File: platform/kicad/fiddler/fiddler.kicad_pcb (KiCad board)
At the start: 2 copper layers, 80 x 78.8 mm, 141 parts, among them J1 5033981892, J2 12402012E212A, J3 Conn_01x04_Pin, J4 Screw_Terminal_01x02, Q1 NPN, Q2 NPN, SW1 SW_Push, SW2 SW_Push, SW3 SW_Push, T1 PT61018PEL, U1 ESP32-WROOM-32E, U2 TAS5731MPHP, U3 LAN8720A, U4 MCP16311x-xMNY, U5 CP2102N-Axx-xQFN24, U6 AP63203WU

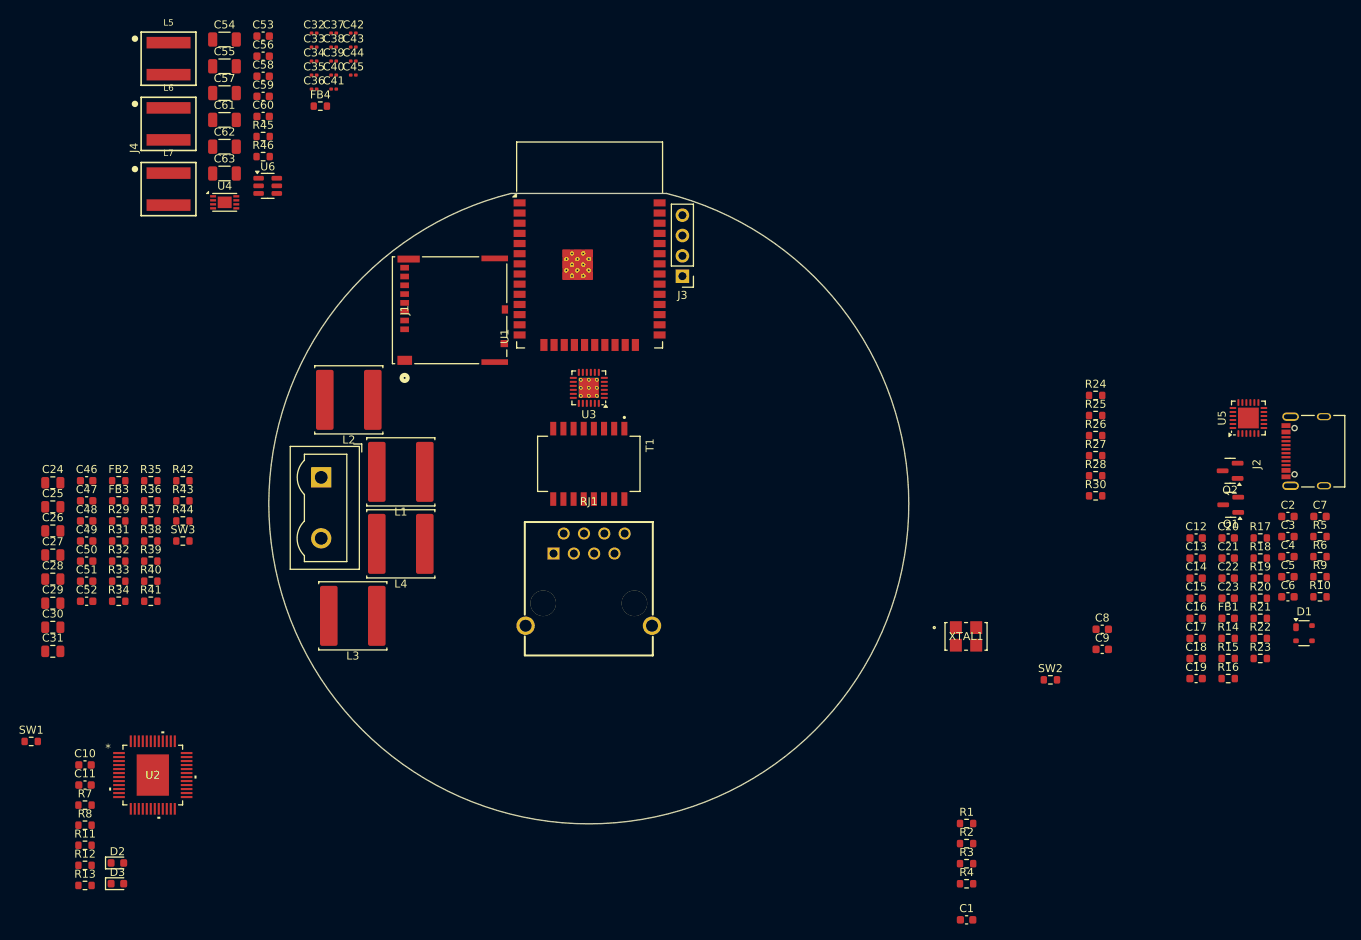
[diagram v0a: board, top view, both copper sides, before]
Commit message: Fiddler Ray Speaker: Complete first revision
This change completes the first iteration schematic and layout for the fiddler ray speaker PCB.
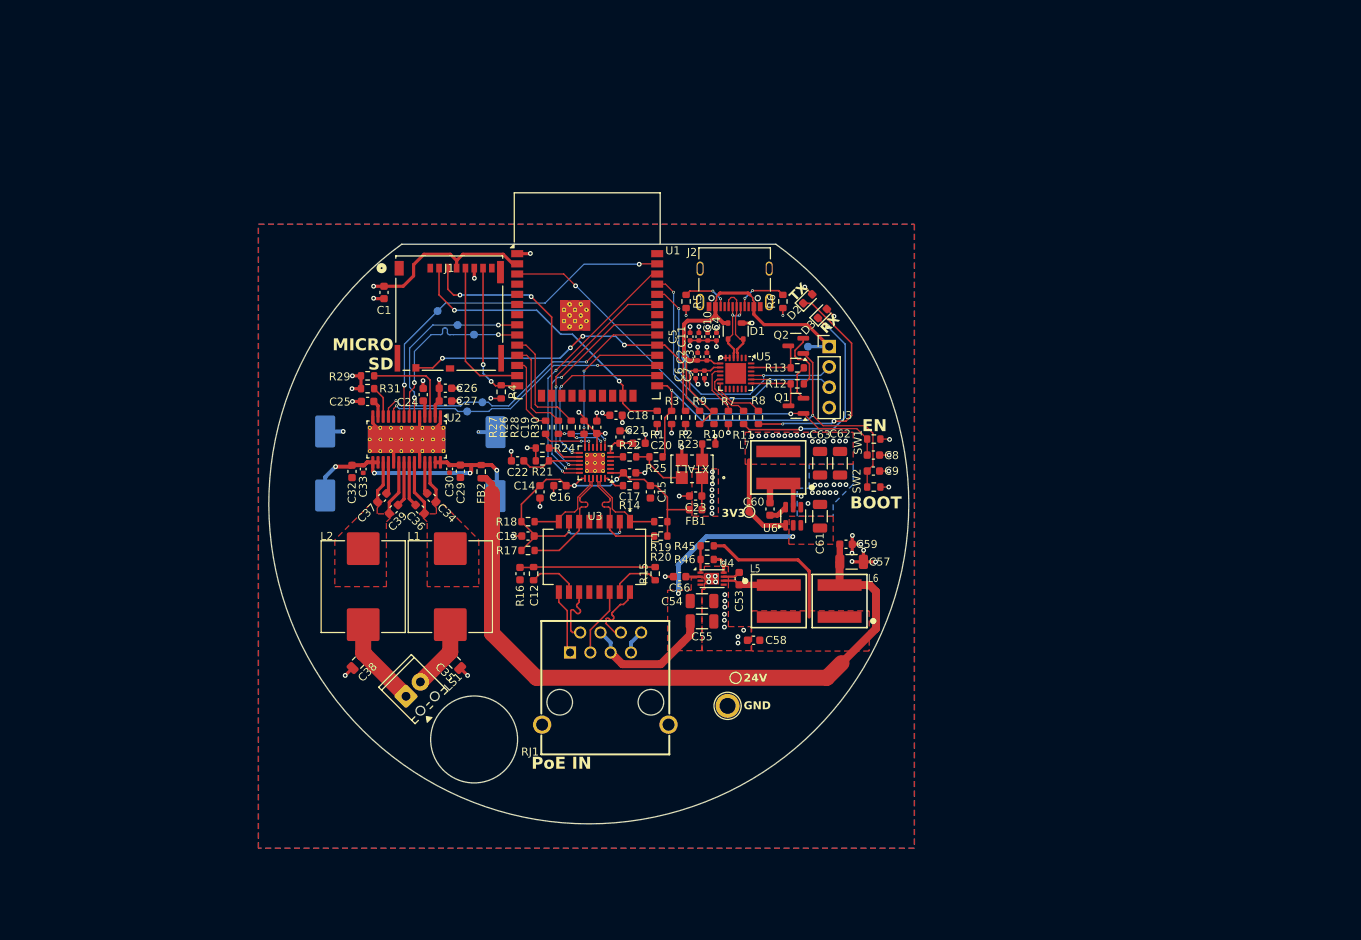
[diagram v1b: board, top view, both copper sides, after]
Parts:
- removed C40, C45: 680n, Capacitor_SMD:C_0201_0603Metric
- removed C41: 4n7, Capacitor_SMD:C_0201_0603Metric
- removed C42, C44: 330p, Capacitor_SMD:C_0201_0603Metric
- removed C43: 2.2n, Capacitor_SMD:C_0201_0603Metric
- removed C46, C48, C50, C51: 100n 10V, Capacitor_SMD:C_0603_1608Metric
- removed C47: 10u 16V, Capacitor_SMD:C_0603_1608Metric
- removed C49: 4u7 6.3V, Capacitor_SMD:C_0603_1608Metric
- removed C52: 1u 25V, Capacitor_SMD:C_0603_1608Metric
- removed FB3, FB4: 120/4A, Resistor_SMD:R_0603_1608Metric
- removed J4: Screw_Terminal_01x02, TerminalBlock:TerminalBlock_Wuerth_691311400102_P7.62mm
- removed L3, L4: 15u, Inductor_SMD:L_Changjiang_FNR8040S
- removed R32, R33, R35, R39: 10k, Resistor_SMD:R_0603_1608Metric
- removed R34: 15k, Resistor_SMD:R_0603_1608Metric
- removed R36: 18k2 1%, Resistor_SMD:R_0603_1608Metric
- removed R37, R38, R42, R43: 18, Resistor_SMD:R_0603_1608Metric
- removed R40, R41: 470, Resistor_SMD:R_0603_1608Metric
- removed R44: 0, Resistor_SMD:R_0603_1608Metric
- removed SW3: SW_Push, Resistor_SMD:R_0603_1608Metric
- added LS1: Speaker, TerminalBlock_Phoenix:TerminalBlock_Phoenix_MPT-0,5-2-2.54_1x02_P2.54mm_Horizontal, F.Cu at (77.2, 124.1)
- added TP1: 24, TestPoint:TestPoint_Pad_D1.0mm, F.Cu at (118.3, 121.8)
- added TP10: SDA, TestPoint:TestPoint_Pad_D1.0mm, B.Cu at (84.8, 88.5)
- added TP2: GND, TestPoint:TestPoint_Plated_Hole_D2.0mm, F.Cu at (117.3, 125.2)
- added TP3: 3V3, TestPoint:TestPoint_Pad_D1.0mm, F.Cu at (120.0, 101.0)
- added TP4: VBUS, TestPoint:TestPoint_Pad_D1.0mm, B.Cu at (127.4, 80.3)
- added TP5: 2V7, TestPoint:TestPoint_Pad_D1.0mm, B.Cu at (112.0, 81.7)
- added TP6: LRCLK, TestPoint:TestPoint_Pad_D1.0mm, B.Cu at (83.6, 77.7)
- added TP7: BLCK, TestPoint:TestPoint_Pad_D1.0mm, B.Cu at (85.7, 78.8)
- added TP8: SDIN, TestPoint:TestPoint_Pad_D1.0mm, B.Cu at (81.1, 75.9)
- added TP9: SCL, TestPoint:TestPoint_Pad_D1.0mm, B.Cu at (86.7, 87.3)
- C10, C11, C2, C3, C4, C5, C6, C7: footprint Capacitor_SMD:C_0603_1608Metric -> Capacitor_SMD:C_0402_1005Metric
- C24: value 100n 50V -> 1u; footprint Capacitor_SMD:C_0805_2012Metric -> Capacitor_SMD:C_0603_1608Metric
- C25: value 220u 35V -> 1u; footprint Capacitor_SMD:C_0805_2012Metric -> Capacitor_SMD:C_0603_1608Metric
- C26: value 100n 50V -> 4u7; footprint Capacitor_SMD:C_0805_2012Metric -> Capacitor_SMD:C_0603_1608Metric
- C27: value 220u 35V -> 100n; footprint Capacitor_SMD:C_0805_2012Metric -> Capacitor_SMD:C_0603_1608Metric
- C28, C31: value 33n -> 390u; footprint Capacitor_SMD:C_0805_2012Metric -> Capacitor_SMD:CP_Elec_10x10; moved to B.Cu
- C29: value 33n -> 22u; footprint Capacitor_SMD:C_0805_2012Metric -> Capacitor_SMD:C_0603_1608Metric
- C30: value 33n -> 100n; footprint Capacitor_SMD:C_0805_2012Metric -> Capacitor_SMD:C_0402_1005Metric
- C32: value 1u -> 22u; footprint Capacitor_SMD:C_0201_0603Metric -> Capacitor_SMD:C_0603_1608Metric
- C33: value 680n -> 100n; footprint Capacitor_SMD:C_0201_0603Metric -> Capacitor_SMD:C_0402_1005Metric
- C34, C36: value 330p -> 220n; footprint Capacitor_SMD:C_0201_0603Metric -> Capacitor_SMD:C_0603_1608Metric
- C35: value 4n7 -> 680n; footprint Capacitor_SMD:C_0201_0603Metric -> Capacitor_SMD:C_0805_2012Metric
- C37, C39: value 47n -> 220n; footprint Capacitor_SMD:C_0201_0603Metric -> Capacitor_SMD:C_0603_1608Metric
- C38: footprint Capacitor_SMD:C_0201_0603Metric -> Capacitor_SMD:C_0805_2012Metric
- FB2: value 120/4A -> FerriteBead
- L1, L2: value 15u -> 10u; footprint Inductor_SMD:L_Changjiang_FNR8040S -> Inductor_SMD:L_Changjiang_FXL1050
- U2: value TAS5731MPHP -> TAS5805MPWP; footprint AusOcean:PHP48_5P17X4P04_TEX -> Package_SO:TSSOP-28-1EP_4.4x9.7mm_P0.65mm_EP3.4x9.7mm_Mask3.1x4.05mm_ThermalVias
- moved D3 113.3 mm to (129.2, 76.2), turned to 45 degrees
- moved SW1 111.9 mm to (135.6, 91.9)
- moved D2 111.4 mm to (127.4, 74.4), turned to 45 degrees
- moved R13 110.1 mm to (126.1, 83.0)
- moved R12 107.5 mm to (126.1, 85.0)
- moved C1 107.0 mm to (74.4, 73.6), turned to -90 degrees
- moved L6 102.9 mm to (131.3, 112.2), turned to 180 degrees
- moved L5 102.1 mm to (123.8, 112.2)
- moved R8 98.4 mm to (121.2, 89.2), turned to 90 degrees
- moved R11 98.2 mm to (119.3, 89.2), turned to 90 degrees
- moved C57 97.9 mm to (132.8, 107.2)
- moved C11 95.0 mm to (113.8, 79.1), turned to 90 degrees
- moved C10 94.5 mm to (114.9, 79.1), turned to 90 degrees
- moved R7 93.9 mm to (117.5, 89.2), turned to 90 degrees
- moved C58 93.4 mm to (120.6, 117.0), turned to 180 degrees
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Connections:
- C1 pad 1: VDD -> +3V3
- C10 pad 1: VDD -> +3V3
- C11 pad 1: VDD -> +3V3
- C13 pad 2: Net-(T1-CT1) -> +3V3A
- C24 pad 1: /Audio/PVDD_AB -> VR_DIG
- C24 pad 2: PGND -> GND
- C25 pad 1: /Audio/PVDD_AB -> AVDD
- C25 pad 2: PGND -> GND
- C26 pad 1: /Audio/PVDD_CD -> +3V3
- C26 pad 2: PGND -> GND
- C27 pad 1: /Audio/PVDD_CD -> +3V3
- C27 pad 2: PGND -> GND
- C28 pad 1: /Audio/OUT_A -> PVDD
- C28 pad 2: /Audio/BST_A -> GND
- C29 pad 1: /Audio/OUT_A -> PVDD
- C29 pad 2: /Audio/BST_B -> GND
- C30 pad 1: /Audio/OUT_C -> PVDD
- C30 pad 2: /Audio/BST_C -> GND
- C31 pad 1: /Audio/OUT_C -> PVDD
- C31 pad 2: /Audio/BST_D -> GND
- C32 pad 1: /Audio/~{RESET} -> PVDD
- C32 pad 2: PGND -> GND
- C33 pad 1: /Audio/SPEAKER+ -> PVDD
- C33 pad 2: PGND -> GND
- C34 pad 1: Net-(C34-Pad1) -> Net-(U2-BST_A+)
- C34 pad 2: PGND -> /Audio/A
- C35 pad 1: Net-(U2A-PLL_FLTM) -> Net-(C35-Pad1)
- C35 pad 2: AVSS -> GND
- C36 pad 1: Net-(C36-Pad1) -> Net-(U2-BST_A-)
- C36 pad 2: PGND -> /Audio/A
- C37 pad 1: Net-(U2A-PLL_FLTM) -> Net-(U2-BST_B+)
- C37 pad 2: Net-(C37-Pad2) -> /Audio/B
- C38 pad 2: PGND -> GND
- C39 pad 1: Net-(C39-Pad1) -> Net-(U2-BST_B-)
- C39 pad 2: /Audio/VR_ANA -> /Audio/B
- C4 pad 1: VDD -> +3V3
- C5 pad 1: VDD -> +3V3
- C62 pad 1: VDD -> +3V3
- C63 pad 1: VDD -> +3V3
- D2 pad 2: VDD -> +3V3
- D3 pad 2: VDD -> +3V3
- FB2 pad 1: /Audio/PVDD -> +24V
- FB2 pad 2: /Audio/PVDD_AB -> PVDD
- J1 pad 4: VDD -> +3V3
- L1 pad 1: /Audio/OUT_A -> /Audio/A
- L1 pad 2: /Audio/SPEAKER+ -> Net-(C35-Pad1)
- L2 pad 1: /Audio/OUT_A -> /Audio/B
- L7 pad 2: VDD -> +3V3
- R1 pad 1: VDD -> +3V3
- R17 pad 2: /Ethernet/RD+ -> /Ethernet/TD+
- R18 pad 2: /Ethernet/RD- -> /Ethernet/TD-
- R19 pad 2: /Ethernet/TD+ -> /Ethernet/RD+
- R2 pad 1: VDD -> +3V3
- R20 pad 2: /Ethernet/TD- -> /Ethernet/RD-
- R29 pad 1: AVDD -> +3V3
- R29 pad 2: /Audio/A_SEL -> /Audio/ADR
- R3 pad 1: VDD -> +3V3
- R3 pad 2: /MCU/I2S_CLK -> /MCU/EMAC_CLK
- R31 pad 1: AVDD -> +3V3
- R31 pad 2: /Audio/PBTL -> /Audio/~{PDN}
- R45 pad 1: Net-(U4-SW) -> Net-(C58-Pad1)
- R7 pad 1: VDD -> +3V3
- T1 pad 1: /Ethernet/TD+ -> /Ethernet/RD+
- T1 pad 11: /Ethernet/RX+ -> /Ethernet/TX-
- T1 pad 14: /Ethernet/TX- -> /Ethernet/RX+
- T1 pad 16: /Ethernet/TX+ -> /Ethernet/RX-
- T1 pad 2: Net-(T1-CT1) -> +3V3A
- T1 pad 3: /Ethernet/TD- -> /Ethernet/RD-
- T1 pad 6: /Ethernet/RD+ -> /Ethernet/TD+
- T1 pad 7: Net-(T1-CT1) -> +3V3A
- T1 pad 8: /Ethernet/RD- -> /Ethernet/TD-
- T1 pad 9: /Ethernet/RX- -> /Ethernet/TX+
- U1 pad 2: VDD -> +3V3
- U1 pad 27: unconnected-(U1-IO16-Pad27) -> /Audio/SDA
- U1 pad 30: unconnected-(U1-IO18-Pad30) -> /Audio/SCL
- U2 pad 1: /Audio/OUT_A -> GND
- U2 pad 10: Net-(U2A-PLL_FLTM) -> /Audio/SDA
- U2 pad 11: Net-(U2A-PLL_FLTP) -> /Audio/SCL
- U2 pad 12: /Audio/VR_ANA -> /Audio/~{PDN}
- U2 pad 13: Net-(U2B-AVDD) -> AVDD
- U2 pad 14: /Audio/A_SEL -> GND
- U2 pad 15: /Audio/BCLK -> PVDD
- U2 pad 16: Net-(U2A-OSC_RES) -> PVDD
- U2 pad 17: PGND -> /Audio/B
- U2 pad 18: VR_DIG -> Net-(U2-BST_B+)
- U2 pad 19: /Audio/~{PDN} -> GND
- U2 pad 2: /Audio/PVDD_AB -> +3V3
- U2 pad 20: /Audio/WS -> /Audio/B
- U2 pad 21: /Audio/SCLK -> Net-(U2-BST_B-)
- U2 pad 22: /Audio/DIN -> Net-(U2-BST_A-)
- U2 pad 23: /Audio/SDA -> /Audio/A
- U2 pad 24: /Audio/SCL -> GND
- U2 pad 25: /Audio/~{RESET} -> Net-(U2-BST_A+)
- U2 pad 26: PGND -> /Audio/A
- U2 pad 27: VDD -> PVDD
- U2 pad 28: PGND -> PVDD
- U2 pad 29: PGND -> GND
- U2 pad 3: /Audio/PVDD_AB -> /Audio/ADR
- U2 pad 4: /Audio/BST_A -> VR_DIG
- U2 pad 5: unconnected-(U2B-NC-Pad5) -> GND
- U2 pad 6: Net-(U2A-SSTIMER) -> /MCU/I2S_WS
- U2 pad 7: unconnected-(U2B-NC-Pad7) -> /MCU/I2S_BCLK
- U2 pad 8: /Audio/PBTL -> /MCU/I2S_DOUT
- U2 pad 9: AVSS -> unconnected-(U2-SDOUT-Pad9)
- U5 pad 5: VDD -> +3V3
- U5 pad 6: VDD -> +3V3
- U6 pad 1: VDD -> +3V3
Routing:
- net +24V: track 0.00 -> 87.3 mm
- net GND: track 0.00 -> 80.2 mm, vias 0 -> 72
- net +3V3: track 0.00 -> 70.7 mm, vias 0 -> 42
- net /MCU/EN: track 0.00 -> 54.3 mm, vias 0 -> 2
- net /MCU/EMAC_CLK: track 0.00 -> 54.0 mm, vias 0 -> 2
- net +3V3A: track 0.00 -> 53.6 mm, vias 0 -> 4
- net VBUS: track 0.00 -> 45.6 mm
- net /MCU/I2S_DOUT: track 0.00 -> 44.8 mm, vias 0 -> 2
- net /MCU/SD_DET: track 0.00 -> 42.5 mm, vias 0 -> 4
- net /Audio/SCL: track 0.00 -> 39.3 mm, vias 0 -> 2
- net /MCU/HSPI_CS: track 0.00 -> 38.0 mm, vias 0 -> 2
- net /MCU/TX: track 0.00 -> 37.3 mm, vias 0 -> 2
- net /Audio/SDA: track 0.00 -> 36.8 mm, vias 0 -> 2
- net Vin: track 0.00 -> 36.2 mm, vias 0 -> 2
- net PVDD: track 0.00 -> 35.6 mm, vias 0 -> 4
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- added copper zone on F.Cu, net +3V3
- added copper zone on In2.Cu, net +3V3
- added copper zone on F.Cu, net /Audio/A
- added copper zone on F.Cu, net /Audio/B
- added copper zone on B.Cu, net GND
- added copper zone on F.Cu, net GND
- added copper zone on In1.Cu, net GND
- added copper zone on F.Cu, net Net-(C58-Pad1)
- added copper zone on F.Cu, net Vin
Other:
- board size 80 x 78.8 mm -> 80 x 72.5 mm
- copper layers 2 -> 4
- board text added: "24V"
- board text added: "3V3"
- board text added: "BCLK"
- board text added: "BOOT"
- board text added: "DOUT"
- board text added: "EN"
- board text added: "GND"
- board text added: "MICRO SD"
- board text added: "PoE IN"
- board text added: "RX"
- board text added: "SCL"
- board text added: "SDA"
- board text added: "TX"
- board text added: "VBUS"
- board text added: "VBUS_BIAS"
- board text added: "WS"

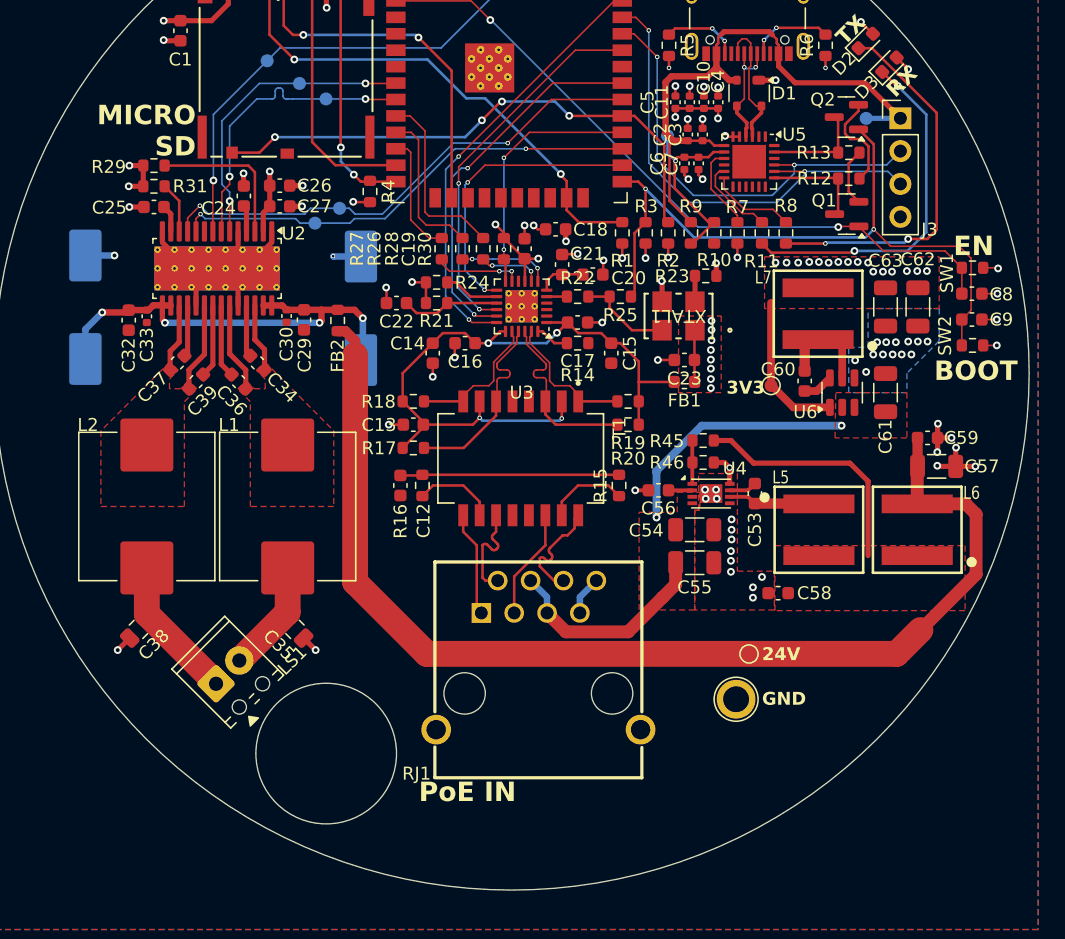
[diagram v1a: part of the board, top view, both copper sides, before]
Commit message: Fiddler Ray Speaker: Finalise Silkscreen
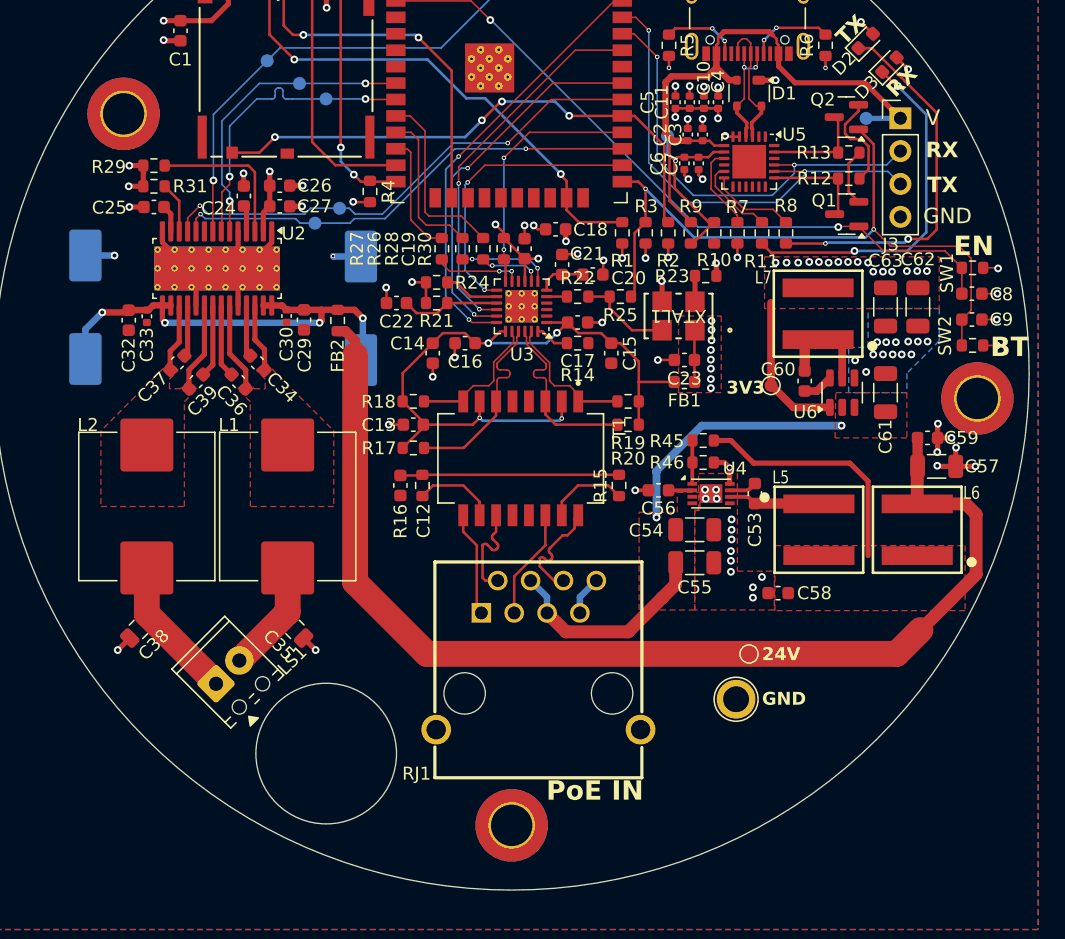
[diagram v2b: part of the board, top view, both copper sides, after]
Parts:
- added H1: MountingHole_Pad, MountingHole:MountingHole_3.2mm_M3_DIN965_Pad_TopBottom, F.Cu at (70.0, 80.0)
- added H2: MountingHole_Pad, MountingHole:MountingHole_3.2mm_M3_DIN965_Pad_TopBottom, F.Cu at (100.0, 135.0)
- added H3: MountingHole_Pad, MountingHole:MountingHole_3.2mm_M3_DIN965_Pad_TopBottom, F.Cu at (136.0, 102.0)
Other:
- board text added: "BT"
- board text added: "Designed by:"
- board text added: "Fiddler Ray"
- board text added: "V"
- board text added: "V1 REVA"
- board text added: "davidsutton@ausocean.org"
- board text removed: "BOOT"
- board text removed: "MICRO SD"

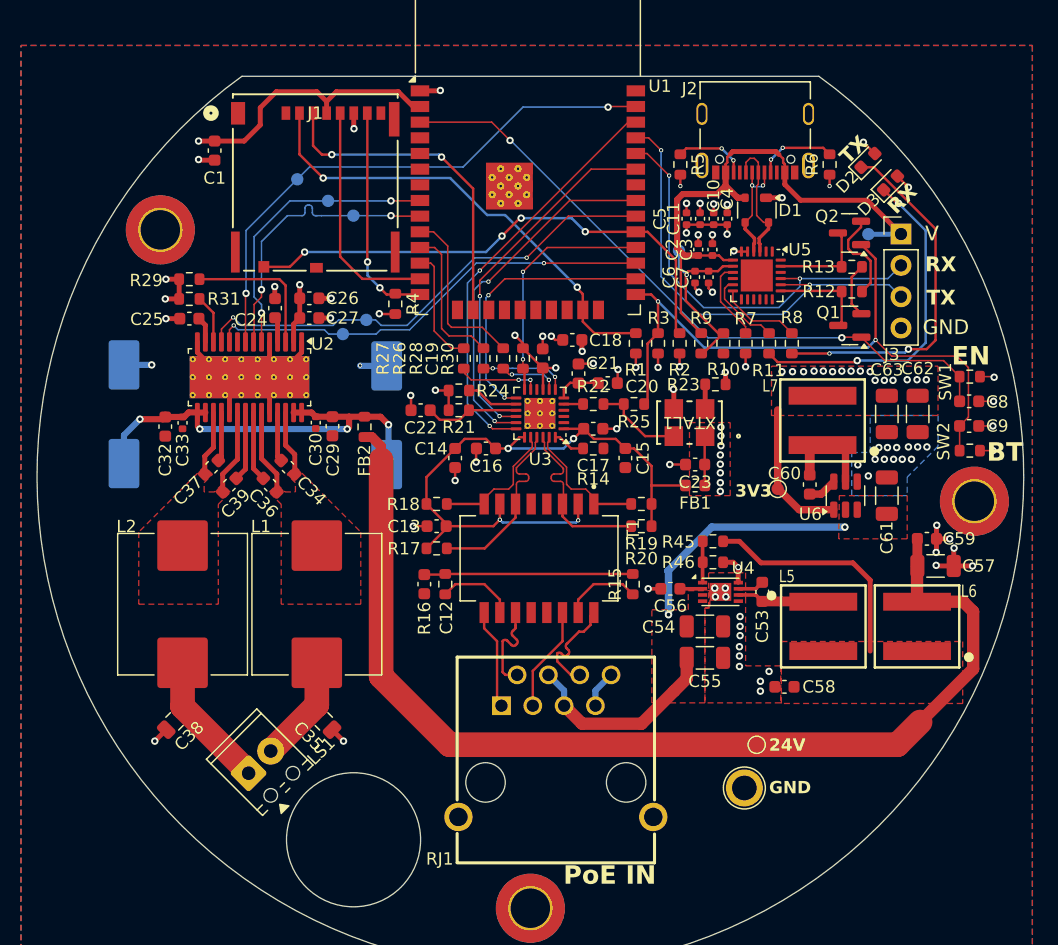
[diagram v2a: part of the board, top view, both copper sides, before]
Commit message: Fiddler Ray Speaker: Production rev A
This change adds additional data to components to populate SPN for
the BOM via JLC
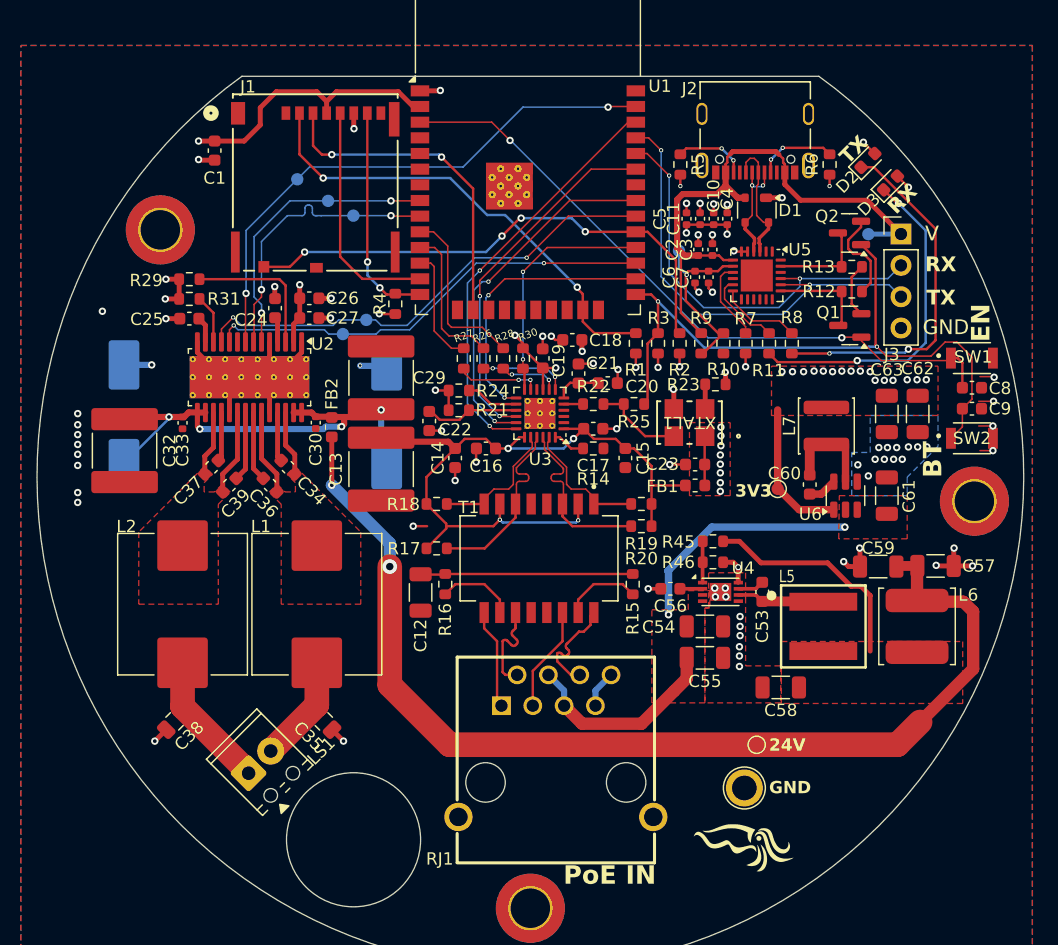
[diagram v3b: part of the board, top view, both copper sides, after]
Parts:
- added G***: LOGO, LOGO, B.Cu at (109.0, 102.5)
- C12: value 1nF 2KV -> 1nF; footprint Capacitor_SMD:C_0603_1608Metric -> Capacitor_SMD:C_1206_3216Metric
- C13, C29, C32: footprint Capacitor_SMD:C_0603_1608Metric -> Capacitor_SMD:C_2220_5750Metric
- C57: value 20u -> 22u
- C58: value 100u -> 22u; footprint Capacitor_SMD:C_0603_1608Metric -> Capacitor_SMD:C_1206_3216Metric
- C59: value 20u -> 22u; footprint Capacitor_SMD:C_0603_1608Metric -> Capacitor_SMD:C_1206_3216Metric
- FB2: footprint Resistor_SMD:R_0603_1608Metric -> Inductor_SMD:L_0603_1608Metric
- L6: footprint AusOcean:WE-XHMI_6060 -> Inductor_SMD:L_TDK_VLS6045EX_VLS6045AF
- L7: footprint AusOcean:WE-XHMI_6060 -> Inductor_SMD:L_Changjiang_FNR4030S
- SW1, SW2: footprint Resistor_SMD:R_0603_1608Metric -> AusOcean:SW_B3U-1000P
- moved C13 6.45 mm to (87.9, 99.4), turned to 90 degrees
- moved C29 5.57 mm to (87.9, 92.0), turned to 90 degrees
- moved C59 4.55 mm to (128.2, 107.3), turned to 180 degrees
- moved C32 3.83 mm to (67.1, 97.9)
- moved FB2 2.65 mm to (83.9, 96.0)
- moved SW1 1.51 mm to (135.8, 90.4)
- moved C9 1.42 mm to (135.8, 94.5)
- moved C8 1.12 mm to (135.8, 92.8)
- moved C22 1.12 mm to (91.8, 95.5), turned to -90 degrees
- moved SW2 1.02 mm to (135.8, 96.9)
- moved C12 0.74 mm to (91.1, 109.4)
- moved L7 0.55 mm to (124.0, 95.9), turned to 90 degrees
- moved C58 0.30 mm to (120.3, 117.1)
- turned L6 to 90 degrees
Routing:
- net +3V3A: track 53.6 -> 59.9 mm
- net PVDD: track 35.6 -> 37.9 mm
- net /MCU/EMAC_CLK: track 54.0 -> 55.3 mm
- net +24V: track 87.3 -> 88.0 mm, vias 0 -> 2
- net Net-(C58-Pad1): track 19.0 -> 18.2 mm
- net GND: track 80.2 -> 79.7 mm, vias 72 -> 76
